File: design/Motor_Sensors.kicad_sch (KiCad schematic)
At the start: 7 parts, among them J8 HALL_ENC, SW1 SENSOR_VOLTAGE

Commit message: Pequeños cambios
Pequeños cambios en esquemático
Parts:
- renumbered R32 to R33, R33 to R34, R34 to R35, R35 to R36
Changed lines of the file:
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@@
 		(dnp no)
 		(fields_autoplaced yes)
-		(property "Reference" "#PWR065"
+		(property "Reference" "#PWR067"
 			(at 129.54 62.23 0)
 			(effects
@@
 			(project "ESCX"
 				(path "/6389d757-a1bd-4c0a-9d55-6114b19cc67a/b1ebc81e-c8d0-4dfc-b018-5639ecb79376"
-					(reference "#PWR065")
+					(reference "#PWR067")
 					(unit 1)
 				)
@@
 		(dnp no)
 		(fields_autoplaced yes)
-		(property "Reference" "R35"
+		(property "Reference" "R36"
 			(at 175.26 78.74 90)
 			(effects
@@
 			(project "ESCX"
 				(path "/6389d757-a1bd-4c0a-9d55-6114b19cc67a/b1ebc81e-c8d0-4dfc-b018-5639ecb79376"
-					(reference "R35")
+					(reference "R36")
 					(unit 1)
 				)
@@
 		(dnp no)
 		(fields_autoplaced yes)
-		(property "Reference" "R33"
+		(property "Reference" "R34"
 			(at 143.51 73.66 90)
 			(effects
@@
 			(project "ESCX"
 				(path "/6389d757-a1bd-4c0a-9d55-6114b19cc67a/b1ebc81e-c8d0-4dfc-b018-5639ecb79376"
-					(reference "R33")
+					(reference "R34")
 					(unit 1)
 				)
@@
 		(dnp no)
 		(fields_autoplaced yes)
-		(property "Reference" "#PWR068"
+		(property "Reference" "#PWR070"
 			(at 181.61 120.65 0)
 			(effects
@@
 			(project "ESCX"
 				(path "/6389d757-a1bd-4c0a-9d55-6114b19cc67a/b1ebc81e-c8d0-4dfc-b018-5639ecb79376"
-					(reference "#PWR068")
+					(reference "#PWR070")
 					(unit 1)
 				)
@@
 		(dnp no)
 		(fields_autoplaced yes)
-		(property "Reference" "R32"
+		(property "Reference" "R33"
 			(at 134.62 71.12 90)
 			(effects
@@
 			(project "ESCX"
 				(path "/6389d757-a1bd-4c0a-9d55-6114b19cc67a/b1ebc81e-c8d0-4dfc-b018-5639ecb79376"
-					(reference "R32")
+					(reference "R33")
 					(unit 1)
 				)
@@
 		(dnp no)
 		(fields_autoplaced yes)
-		(property "Reference" "#PWR067"
+		(property "Reference" "#PWR069"
 			(at 181.61 77.47 0)
 			(effects
@@
 			(project "ESCX"
 				(path "/6389d757-a1bd-4c0a-9d55-6114b19cc67a/b1ebc81e-c8d0-4dfc-b018-5639ecb79376"
-					(reference "#PWR067")
+					(reference "#PWR069")
 					(unit 1)
 				)
@@
 		(dnp no)
 		(fields_autoplaced yes)
-		(property "Reference" "R34"
+		(property "Reference" "R35"
 			(at 153.67 76.2 90)
 			(effects
@@
 			(project "ESCX"
 				(path "/6389d757-a1bd-4c0a-9d55-6114b19cc67a/b1ebc81e-c8d0-4dfc-b018-5639ecb79376"
-					(reference "R34")
+					(reference "R35")
 					(unit 1)
 				)
@@
 		(dnp no)
 		(fields_autoplaced yes)
-		(property "Reference" "#PWR064"
+		(property "Reference" "#PWR066"
 			(at 124.46 62.23 0)
 			(effects
@@
 			(project "ESCX"
 				(path "/6389d757-a1bd-4c0a-9d55-6114b19cc67a/b1ebc81e-c8d0-4dfc-b018-5639ecb79376"
-					(reference "#PWR064")
+					(reference "#PWR066")
 					(unit 1)
 				)
@@
 		(dnp no)
 		(fields_autoplaced yes)
-		(property "Reference" "#PWR066"
+		(property "Reference" "#PWR068"
 			(at 156.21 87.63 0)
 			(effects
@@
 			(project "ESCX"
 				(path "/6389d757-a1bd-4c0a-9d55-6114b19cc67a/b1ebc81e-c8d0-4dfc-b018-5639ecb79376"
-					(reference "#PWR066")
+					(reference "#PWR068")
 					(unit 1)
 				)

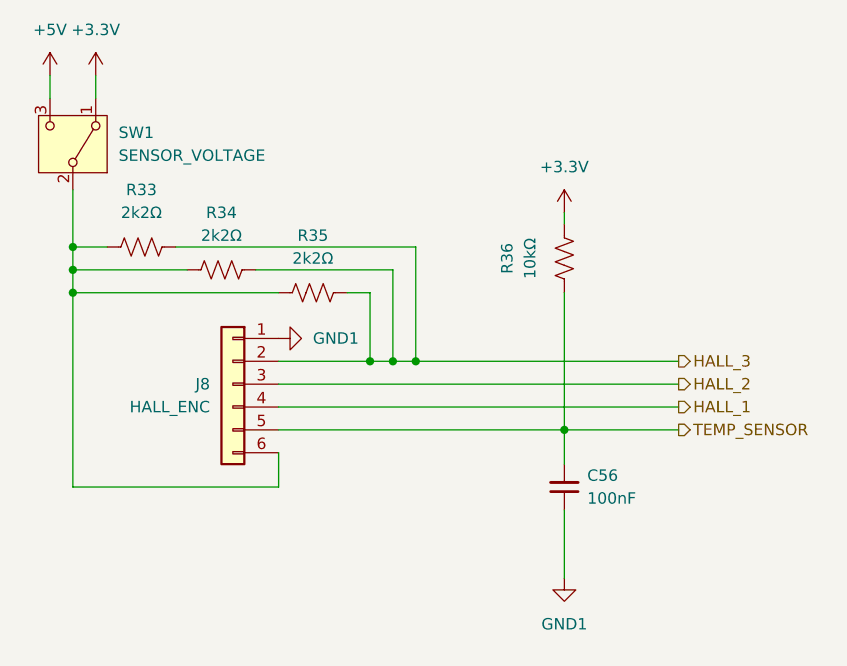
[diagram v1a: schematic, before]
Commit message: Arreglos y cambios
Cambios en ruteos, dimensión de la placa, tamaño de las vías, parámetros de diseño jlcpb (constraints). Agregado de pad térmico de transistores, duplicado de capa inferior y superior para mejor disipación.
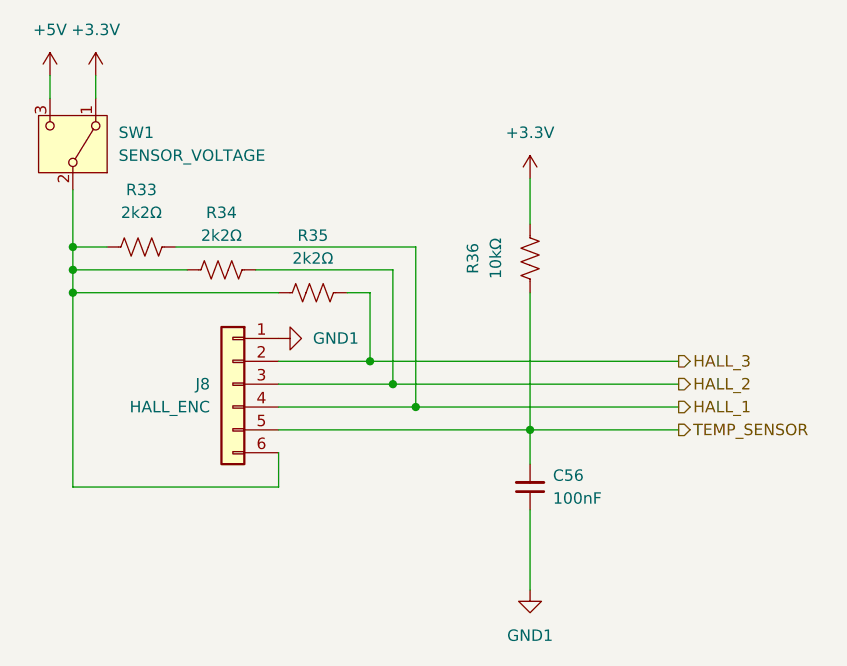
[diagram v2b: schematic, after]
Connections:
- net HALL_1: now also R33.1
- net HALL_2: now also R34.1
- net HALL_3: no longer R33.1, R34.1
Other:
- moved on the sheet: C56, R36

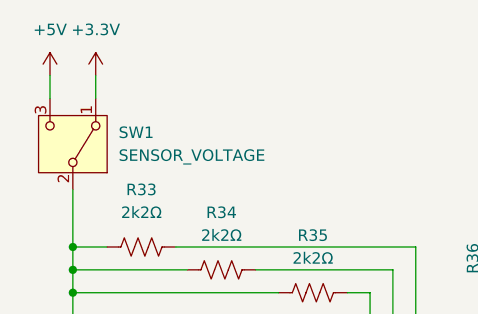
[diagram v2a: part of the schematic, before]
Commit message: cambios en ruteo
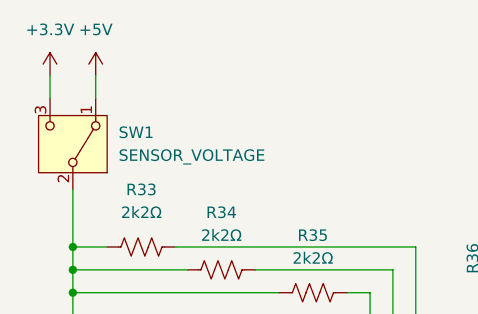
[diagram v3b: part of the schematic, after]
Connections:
- net +3.3V: now also SW1.3 (C); no longer SW1.1 (A)
- net +5V: now also SW1.1 (A); no longer SW1.3 (C)
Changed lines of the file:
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@@
-	)
-	(symbol
-		(lib_id "power:+3.3V")
-		(at 129.54 58.42 0)
-		(unit 1)
-		(exclude_from_sim no)
-		(in_bom yes)
-		(on_board yes)
-		(dnp no)
-		(fields_autoplaced yes)
-		(property "Reference" "#PWR067"
-			(at 129.54 62.23 0)
-			(effects
-				(font
-					(size 1.27 1.27)
-				)
-				(hide yes)
-			)
-		)
-		(property "Value" "+3.3V"
-			(at 129.54 53.34 0)
-			(effects
-				(font
-					(size 1.27 1.27)
-				)
-			)
-		)
-		(property "Footprint" ""
-			(at 129.54 58.42 0)
-			(effects
-				(font
-					(size 1.27 1.27)
-				)
-				(hide yes)
-			)
-		)
-		(property "Datasheet" ""
-			(at 129.54 58.42 0)
-			(effects
-				(font
-					(size 1.27 1.27)
-				)
-				(hide yes)
-			)
-		)
-		(property "Description" "Power symbol creates a global label with name \"+3.3V\""
-			(at 129.54 58.42 0)
-			(effects
-				(font
-					(size 1.27 1.27)
-				)
-				(hide yes)
-			)
-		)
-		(pin "1"
-		)
-		(instances
-			(project "ESCX"
-				(path "/6389d757-a1bd-4c0a-9d55-6114b19cc67a/b1ebc81e-c8d0-4dfc-b018-5639ecb79376"
-					(reference "#PWR067")
-					(unit 1)
-				)
-			)
-		)
 	)
 	(symbol
@@
 				(path "/6389d757-a1bd-4c0a-9d55-6114b19cc67a/b1ebc81e-c8d0-4dfc-b018-5639ecb79376"
 					(reference "R36")
+					(unit 1)
+				)
+			)
+		)
+	)
+	(symbol
+		(lib_id "power:+3.3V")
+		(at 124.46 58.42 0)
+		(unit 1)
+		(exclude_from_sim no)
+		(in_bom yes)
+		(on_board yes)
+		(dnp no)
+		(fields_autoplaced yes)
+		(property "Reference" "#PWR067"
+			(at 124.46 62.23 0)
+			(effects
+				(font
+					(size 1.27 1.27)
+				)
+				(hide yes)
+			)
+		)
+		(property "Value" "+3.3V"
+			(at 124.46 53.34 0)
+			(effects
+				(font
+					(size 1.27 1.27)
+				)
+			)
+		)
+		(property "Footprint" ""
+			(at 124.46 58.42 0)
+			(effects
+				(font
+					(size 1.27 1.27)
+				)
+				(hide yes)
+			)
+		)
+		(property "Datasheet" ""
+			(at 124.46 58.42 0)
+			(effects
+				(font
+					(size 1.27 1.27)
+				)
+				(hide yes)
+			)
+		)
+		(property "Description" "Power symbol creates a global label with name \"+3.3V\""
+			(at 124.46 58.42 0)
+			(effects
+				(font
+					(size 1.27 1.27)
+				)
+				(hide yes)
+			)
+		)
+		(pin "1"
+		)
+		(instances
+			(project "ESCX"
+				(path "/6389d757-a1bd-4c0a-9d55-6114b19cc67a/b1ebc81e-c8d0-4dfc-b018-5639ecb79376"
+					(reference "#PWR067")
 					(unit 1)
 				)
@@
 	)
 	(symbol
+		(lib_id "power:+5V")
+		(at 129.54 58.42 0)
+		(unit 1)
+		(exclude_from_sim no)
+		(in_bom yes)
+		(on_board yes)
+		(dnp no)
+		(fields_autoplaced yes)
+		(property "Reference" "#PWR066"
+			(at 129.54 62.23 0)
+			(effects
+				(font
+					(size 1.27 1.27)
+				)
+				(hide yes)
+			)
+		)
+		(property "Value" "+5V"
+			(at 129.54 53.34 0)
+			(effects
+				(font
+					(size 1.27 1.27)
+				)
+			)
+		)
+		(property "Footprint" ""
+			(at 129.54 58.42 0)
+			(effects
+				(font
+					(size 1.27 1.27)
+				)
+				(hide yes)
+			)
+		)
+		(property "Datasheet" ""
+			(at 129.54 58.42 0)
+			(effects
+				(font
+					(size 1.27 1.27)
+				)
+				(hide yes)
+			)
+		)
+		(property "Description" "Power symbol creates a global label with name \"+5V\""
+			(at 129.54 58.42 0)
+			(effects
+				(font
+					(size 1.27 1.27)
+				)
+				(hide yes)
+			)
+		)
+		(pin "1"
+		)
+		(instances
+			(project "ESCX"
+				(path "/6389d757-a1bd-4c0a-9d55-6114b19cc67a/b1ebc81e-c8d0-4dfc-b018-5639ecb79376"
+					(reference "#PWR066")
+					(unit 1)
+				)
+			)
+		)
+	)
+	(symbol
 		(lib_id "power:+3.3V")
 		(at 177.8 69.85 0)
@@
 					(unit 1)
 				)
-			)
-		)
-	)
-	(symbol
-		(lib_id "power:+5V")
-		(at 124.46 58.42 0)
-		(unit 1)
-		(exclude_from_sim no)
-		(in_bom yes)
-		(on_board yes)
-		(dnp no)
-		(fields_autoplaced yes)
-		(property "Reference" "#PWR066"
-			(at 124.46 62.23 0)
-			(effects
-				(font
-					(size 1.27 1.27)
-				)
-				(hide yes)
-			)
-		)
-		(property "Value" "+5V"
-			(at 124.46 53.34 0)
-			(effects
-				(font
-					(size 1.27 1.27)
-				)
-			)
-		)
-		(property "Footprint" ""
-			(at 124.46 58.42 0)
-			(effects
-				(font
-					(size 1.27 1.27)
-				)
-				(hide yes)
-			)
-		)
-		(property "Datasheet" ""
-			(at 124.46 58.42 0)
-			(effects
-				(font
-					(size 1.27 1.27)
-				)
-				(hide yes)
-			)
-		)
-		(property "Description" "Power symbol creates a global label with name \"+5V\""
-			(at 124.46 58.42 0)
-			(effects
-				(font
-					(size 1.27 1.27)
-				)
-				(hide yes)
-			)
-		)
-		(pin "1"
-		)
-		(instances
-			(project "ESCX"
-				(path "/6389d757-a1bd-4c0a-9d55-6114b19cc67a/b1ebc81e-c8d0-4dfc-b018-5639ecb79376"
-					(reference "#PWR066")
-					(unit 1)
-				)
